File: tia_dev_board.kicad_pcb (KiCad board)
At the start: 2 copper layers, 55.9 x 61 mm, 31 parts, among them J1 Conn_Coaxial, J2 Conn_Coaxial, J3 Conn_Coaxial, U1 PWR_JACK_POS, U2 PWR_JACK_GND, U3 PWR_JACK_NEG, U4 ADA4625-1

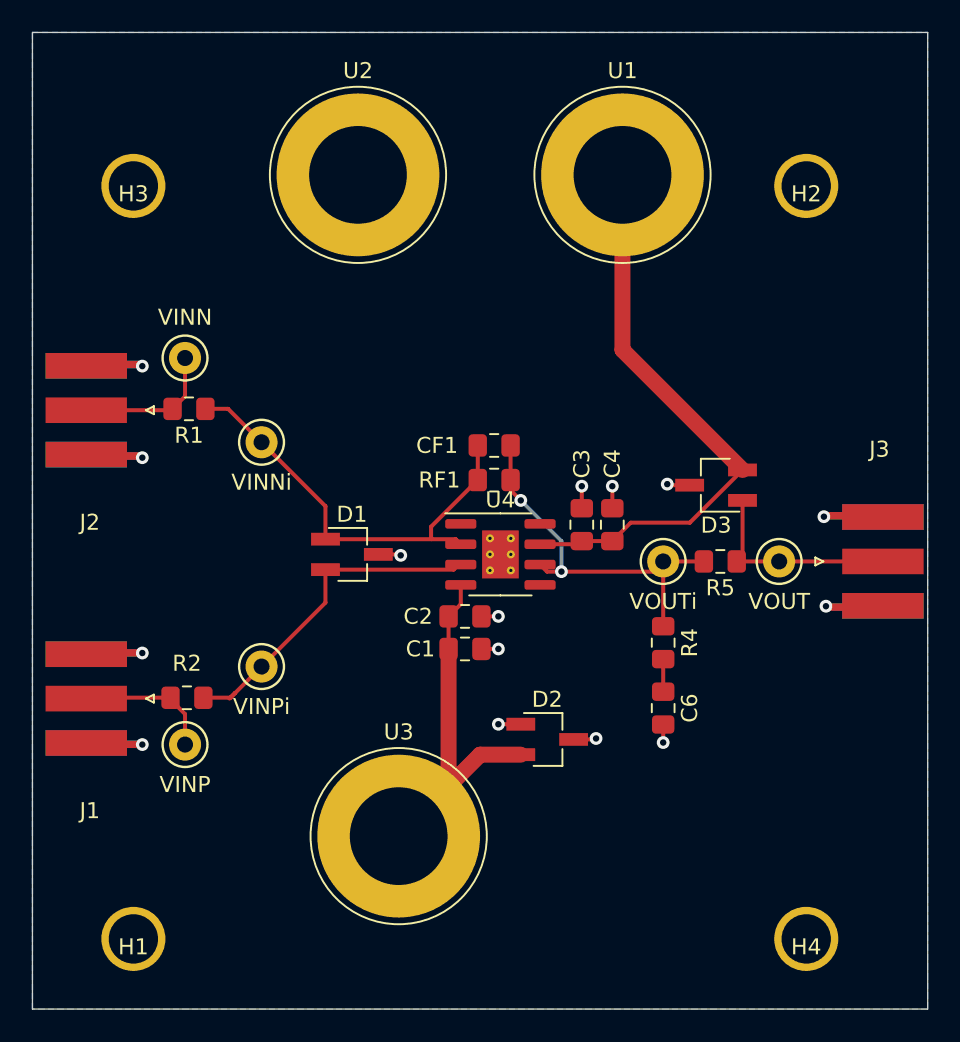
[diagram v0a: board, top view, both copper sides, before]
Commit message: revised PCB according to issues found in version 1
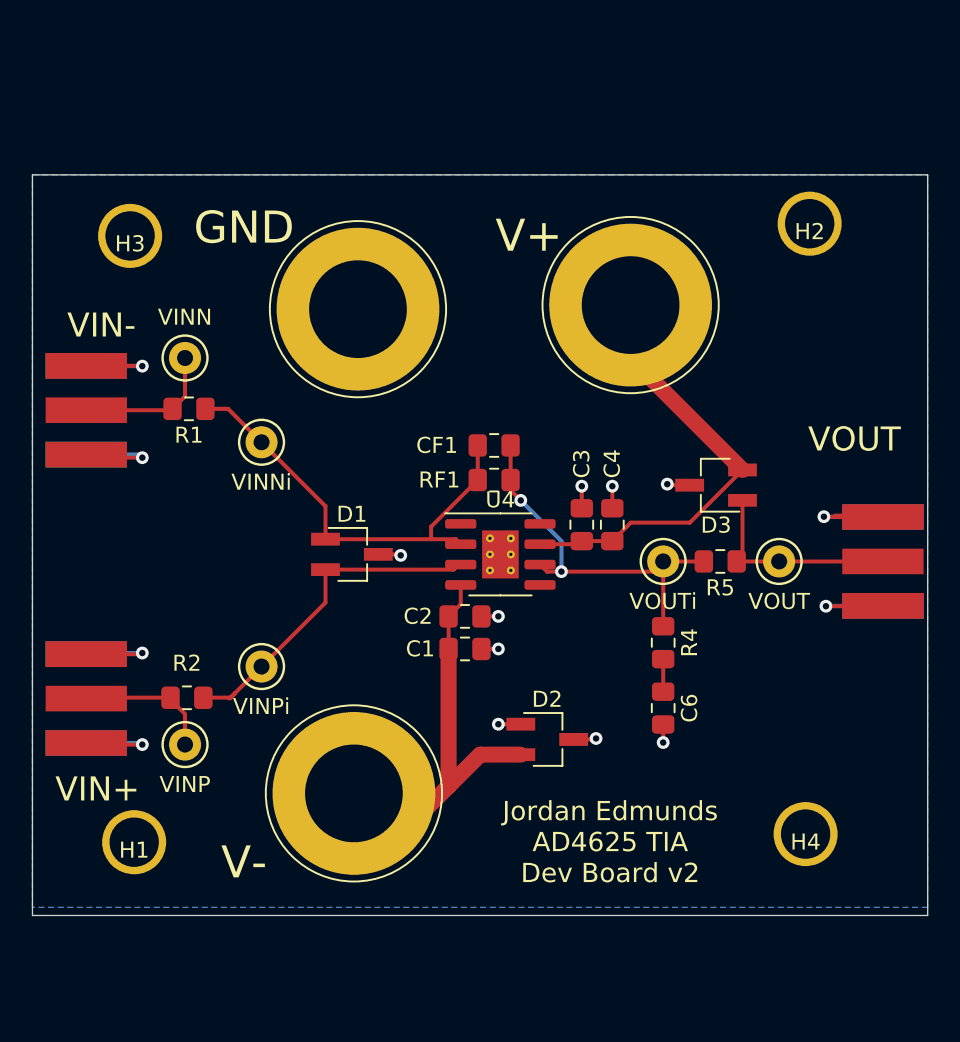
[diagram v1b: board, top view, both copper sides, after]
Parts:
- moved U2 8.38 mm to (160.0, 75.7)
- moved U1 8.14 mm to (177.0, 75.4)
- moved H4 6.54 mm to (188.0, 108.5)
- moved H1 6.03 mm to (146.1, 109.0)
- moved U3 3.86 mm to (159.8, 105.9)
- moved H3 3.13 mm to (145.8, 71.1)
- moved H2 2.37 mm to (188.2, 70.4)
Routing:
- net /V+: track 36.1 -> 25.2 mm
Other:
- board size 55.9 x 61 mm -> 55.9 x 46.2 mm
- board text added: "GND"
- board text added: "Jordan Edmunds AD4625 TIA Dev Board v2"
- board text added: "V+"
- board text added: "V-"
- board text added: "VIN+"
- board text added: "VIN-"
- board text added: "VOUT"
